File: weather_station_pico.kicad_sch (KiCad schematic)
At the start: 16 parts, among them J1 POWER, J3 WDIR, Q1 AO3401A, SW1 SW_Push, U1 LM7805_TO220, U2 E220-900T22D, U3 Pico

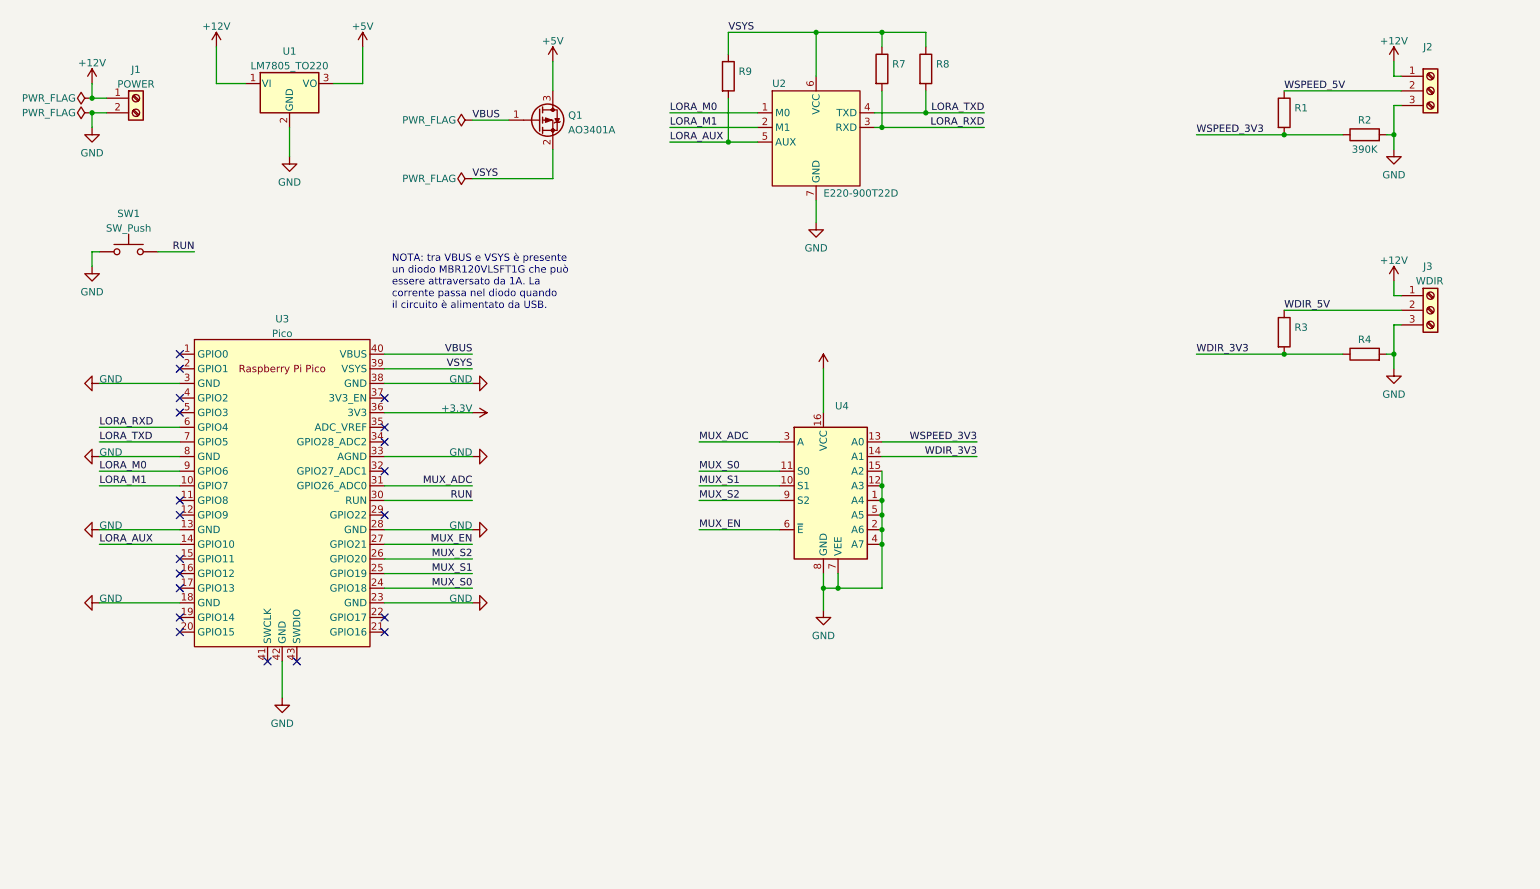
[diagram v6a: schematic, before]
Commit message: add i2c
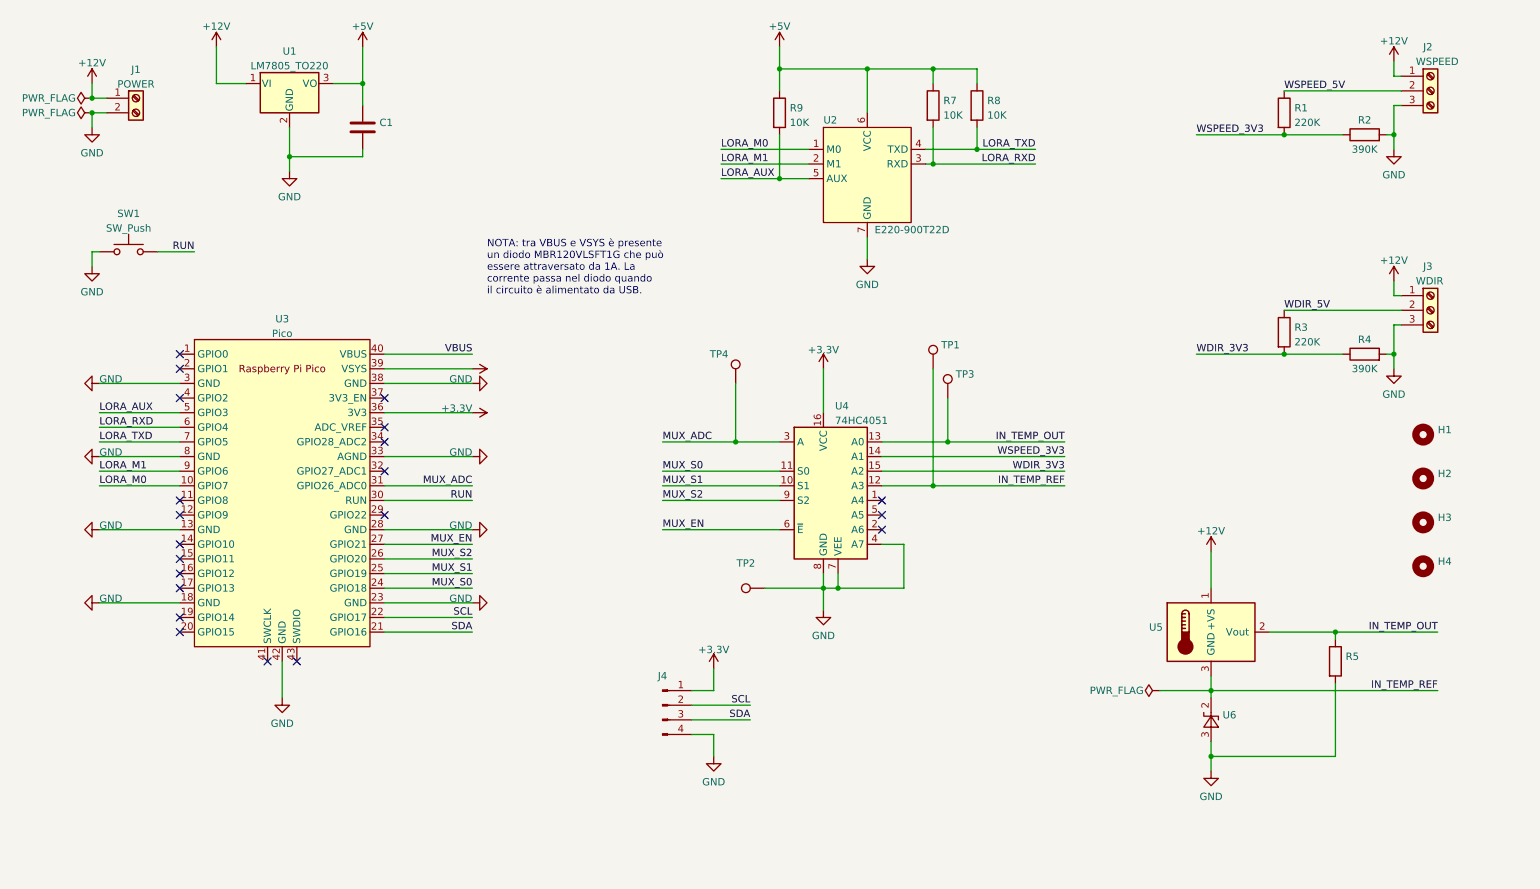
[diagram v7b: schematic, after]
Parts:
- removed Q1: AO3401A, Package_TO_SOT_SMD:SOT-23, symbol Transistor_FET:AO3401A
- added C1: (no value), symbol Device:C
- added H1, H2, H3, H4: (no value), symbol Mechanical:MountingHole
- added J4: (no value), symbol Connector:Conn_01x04_Male
- added R5: (no value), symbol Device:R
- added TP1: (no value), symbol Connector:TestPoint
- added TP2, TP3, TP4: (no value), TestPoint:TestPoint_Pad_D1.5mm, symbol Connector:TestPoint
- added U5: (no value), symbol Sensor_Temperature:LM35-LP
- added U6: (no value), symbol Reference_Voltage:LM385BZ-1.2
- J1: footprint (none) -> TerminalBlock_TE-Connectivity:TerminalBlock_TE_282834-2_1x02_P2.54mm_Horizontal
- J2: value (none) -> WSPEED; footprint (none) -> TerminalBlock_TE-Connectivity:TerminalBlock_TE_282834-3_1x03_P2.54mm_Horizontal
- J3: footprint (none) -> TerminalBlock_TE-Connectivity:TerminalBlock_TE_282834-3_1x03_P2.54mm_Horizontal
- R1, R3: value (none) -> 220K; footprint (none) -> Resistor_THT:R_Axial_DIN0207_L6.3mm_D2.5mm_P10.16mm_Horizontal
- R2: footprint (none) -> Resistor_THT:R_Axial_DIN0207_L6.3mm_D2.5mm_P10.16mm_Horizontal
- R4: value (none) -> 390K; footprint (none) -> Resistor_THT:R_Axial_DIN0207_L6.3mm_D2.5mm_P10.16mm_Horizontal
- R7, R8, R9: value (none) -> 10K; footprint (none) -> Resistor_THT:R_Axial_DIN0207_L6.3mm_D2.5mm_P10.16mm_Horizontal
- U3: footprint RPi_Pico:RPi_Pico_SMD_TH -> MCU_RaspberryPi_and_Boards:RPi_Pico_SMD_TH
- U4: value (none) -> 74HC4051; footprint (none) -> Package_DIP:DIP-16_W7.62mm
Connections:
- net VSYS is gone; now on net +5V: R7.1, R8.1, R9.1, U2.6 (VCC), U3.39 (VSYS)
- net +12V: now also U5.1 (+VS)
- net +3V3: now also J4.1 (Pin_1)
- net +5V: now also C1.1
- net GND: now also C1.2, J4.4 (Pin_4), R5.2, TP2.1, U6.3 (A); no longer U4.1 (A4), U4.12 (A3), U4.15 (A2), U4.2 (A6), U4.5 (A5)
- net LORA_AUX: now also U3.5 (GPIO3); no longer U3.14 (GPIO10)
- net LORA_M0: now also U3.10 (GPIO7); no longer U3.9 (GPIO6)
- net LORA_M1: now also U3.9 (GPIO6); no longer U3.10 (GPIO7)
- net MUX_ADC: now also TP4.1
- net WDIR_3V3: now also U4.15 (A2); no longer U4.14 (A1)
- net WSPEED_3V3: now also U4.14 (A1); no longer U4.13 (A0)
- net SDA: now reaches U3.21 (GPIO16)
- net SDA: now also J4.3 (Pin_3)
- net SCL: now reaches U3.22 (GPIO17)
- net SCL: now also J4.2 (Pin_2)
- new net IN_TEMP_OUT: R5.1, TP3.1, U4.13 (A0), U5.2 (Vout)
- new net IN_TEMP_REF: TP1.1, U4.12 (A3), U5.3 (GND), U6.2 (K)
- no-connect marks 20 -> 21
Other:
- moved on the sheet: R7, R8, R9, U2

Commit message: add i2c pull-up resistors
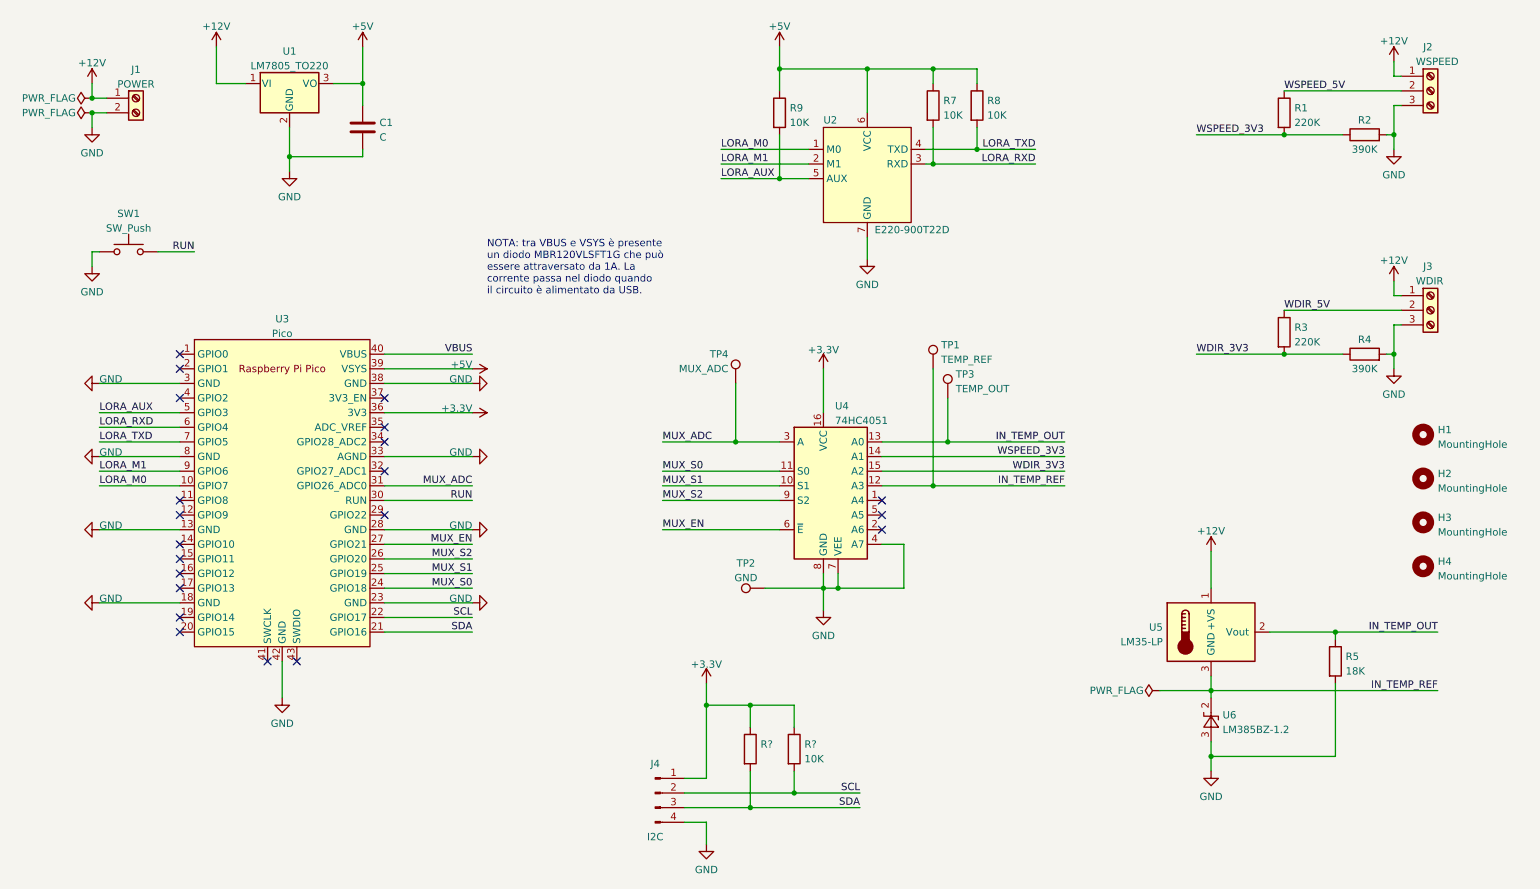
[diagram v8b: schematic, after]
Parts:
- added R?: (no value), Resistor_THT:R_Axial_DIN0207_L6.3mm_D2.5mm_P10.16mm_Horizontal, symbol Device:R
- added R?: 10K, Resistor_THT:R_Axial_DIN0207_L6.3mm_D2.5mm_P10.16mm_Horizontal, symbol Device:R
- C1: value (none) -> C; footprint (none) -> Capacitor_THT:C_Disc_D5.0mm_W2.5mm_P5.00mm
- H1, H2, H3, H4: value (none) -> MountingHole; footprint (none) -> MountingHole:MountingHole_3.2mm_M3
- J4: value (none) -> I2C; footprint (none) -> Connector_JST:JST_XH_B4B-XH-A_1x04_P2.50mm_Vertical
- R5: value (none) -> 18K; footprint (none) -> Resistor_THT:R_Axial_DIN0207_L6.3mm_D2.5mm_P10.16mm_Horizontal
- TP1: value (none) -> TEMP_REF; footprint (none) -> TestPoint:TestPoint_Pad_D1.5mm
- TP2: value (none) -> GND
- TP3: value (none) -> TEMP_OUT
- TP4: value (none) -> MUX_ADC
- U5: value (none) -> LM35-LP; footprint (none) -> Package_TO_SOT_THT:TO-92L_Inline_Wide
- U6: value (none) -> LM385BZ-1.2; footprint (none) -> Package_TO_SOT_THT:TO-92_Inline
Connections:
- net +3V3: now also R?.1, R?.1
- net SCL: now also R?.2
- net SDA: now also R?.2
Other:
- moved on the sheet: J4
